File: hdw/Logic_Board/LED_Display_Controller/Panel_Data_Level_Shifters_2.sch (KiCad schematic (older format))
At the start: 62 parts, among them U2701 74HCT541, U2702 74HCT541

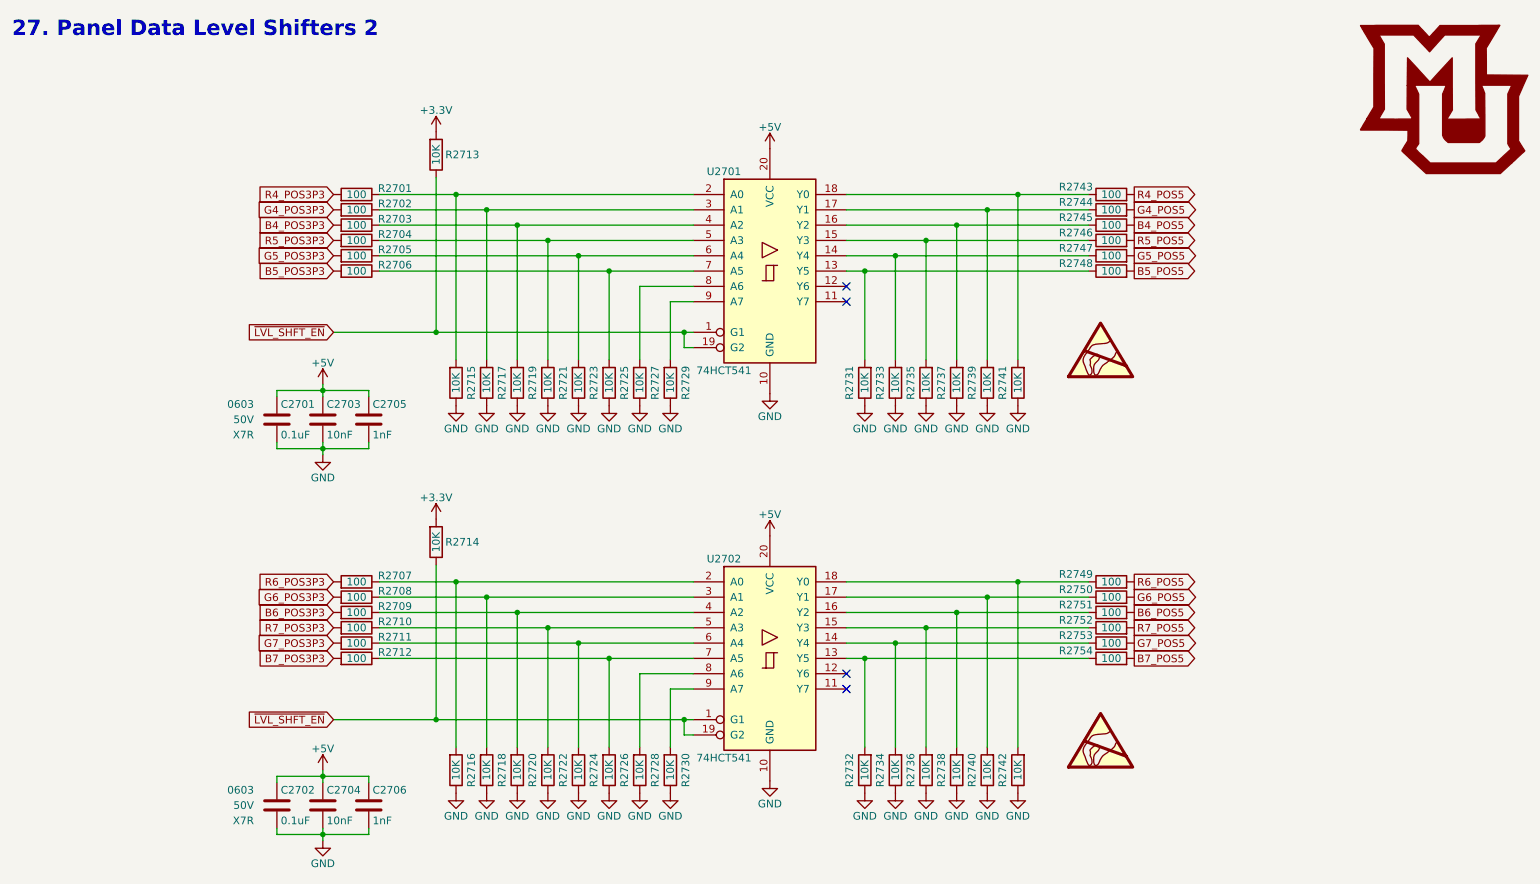
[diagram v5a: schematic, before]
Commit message: Resolved panel data connector orientation issues
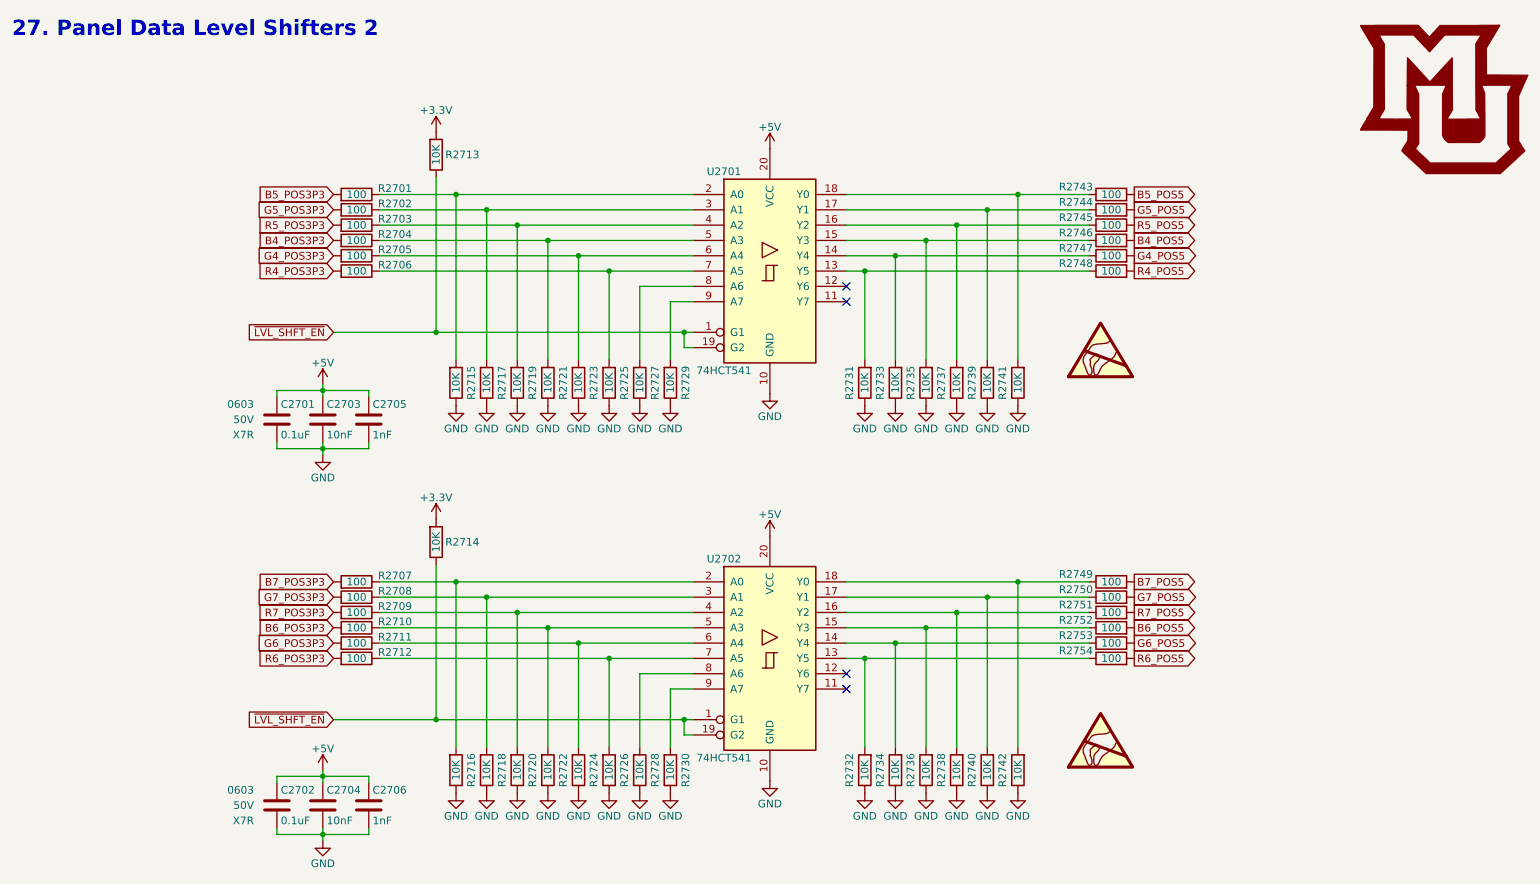
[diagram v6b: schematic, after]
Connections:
- net B4_POS3P3: now also R2704.1; no longer R2703.1
- net B4_POS5: now also R2746.1; no longer R2745.1
- net B5_POS3P3: now also R2701.1; no longer R2706.1
- net B5_POS5: now also R2743.1; no longer R2748.1
- net B6_POS3P3: now also R2710.1; no longer R2709.1
- net B6_POS5: now also R2752.1; no longer R2751.1
- net B7_POS3P3: now also R2707.1; no longer R2712.1
- net B7_POS5: now also R2749.1; no longer R2754.1
- net G4_POS3P3: now also R2705.1; no longer R2702.1
- net G4_POS5: now also R2747.1; no longer R2744.1
- net G5_POS3P3: now also R2702.1; no longer R2705.1
- net G5_POS5: now also R2744.1; no longer R2747.1
- net G6_POS3P3: now also R2711.1; no longer R2708.1
- net G6_POS5: now also R2753.1; no longer R2750.1
- net G7_POS3P3: now also R2708.1; no longer R2711.1
- net G7_POS5: now also R2750.1; no longer R2753.1
- net R4_POS3P3: now also R2706.1; no longer R2701.1
- net R4_POS5: now also R2748.1; no longer R2743.1
- net R5_POS3P3: now also R2703.1; no longer R2704.1
- net R5_POS5: now also R2745.1; no longer R2746.1
- net R6_POS3P3: now also R2712.1; no longer R2707.1
- net R6_POS5: now also R2754.1; no longer R2749.1
- net R7_POS3P3: now also R2709.1; no longer R2710.1
- net R7_POS5: now also R2751.1; no longer R2752.1
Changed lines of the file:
@@
 Wire Wire Line
 	4650 2320 4650 2800
+Text GLabel 7880 2220 2    50   Output ~ 0
+R4_POS5
+Text GLabel 7880 1920 2    50   Output ~ 0
+R5_POS5
+Text GLabel 7880 2020 2    50   Output ~ 0
+B4_POS5
 Text GLabel 7880 1720 2    50   Output ~ 0
-R4_POS5
-Text GLabel 7880 2020 2    50   Output ~ 0
-R5_POS5
-Text GLabel 7880 1920 2    50   Output ~ 0
-B4_POS5
-Text GLabel 7880 2220 2    50   Output ~ 0
 B5_POS5
+Text GLabel 7880 2120 2    50   Output ~ 0
+G4_POS5
 Text GLabel 7880 1820 2    50   Output ~ 0
-G4_POS5
-Text GLabel 7880 2120 2    50   Output ~ 0
 G5_POS5
 $Comp
@@
 Wire Wire Line
 	2950 2020 4050 2020
+Text GLabel 2650 2220 0    50   Input ~ 0
+R4_POS3P3
+Text GLabel 2650 1920 0    50   Input ~ 0
+R5_POS3P3
+Text GLabel 2650 2020 0    50   Input ~ 0
+B4_POS3P3
 Text GLabel 2650 1720 0    50   Input ~ 0
-R4_POS3P3
-Text GLabel 2650 2020 0    50   Input ~ 0
-R5_POS3P3
-Text GLabel 2650 1920 0    50   Input ~ 0
-B4_POS3P3
-Text GLabel 2650 2220 0    50   Input ~ 0
 B5_POS3P3
+Text GLabel 2650 2120 0    50   Input ~ 0
+G4_POS3P3
 Text GLabel 2650 1820 0    50   Input ~ 0
-G4_POS3P3
-Text GLabel 2650 2120 0    50   Input ~ 0
 G5_POS3P3
 Wire Wire Line
@@
 Wire Wire Line
 	4650 4850 4650 5330
+Text GLabel 7880 4750 2    50   Output ~ 0
+R6_POS5
+Text GLabel 7880 4450 2    50   Output ~ 0
+R7_POS5
+Text GLabel 7880 4550 2    50   Output ~ 0
+B6_POS5
 Text GLabel 7880 4250 2    50   Output ~ 0
-R6_POS5
-Text GLabel 7880 4550 2    50   Output ~ 0
-R7_POS5
-Text GLabel 7880 4450 2    50   Output ~ 0
-B6_POS5
-Text GLabel 7880 4750 2    50   Output ~ 0
 B7_POS5
+Text GLabel 7880 4650 2    50   Output ~ 0
+G6_POS5
 Text GLabel 7880 4350 2    50   Output ~ 0
-G6_POS5
-Text GLabel 7880 4650 2    50   Output ~ 0
 G7_POS5
 $Comp
@@
 Wire Wire Line
 	2950 4550 4050 4550
+Text GLabel 2650 4750 0    50   Input ~ 0
+R6_POS3P3
+Text GLabel 2650 4450 0    50   Input ~ 0
+R7_POS3P3
+Text GLabel 2650 4550 0    50   Input ~ 0
+B6_POS3P3
 Text GLabel 2650 4250 0    50   Input ~ 0
-R6_POS3P3
-Text GLabel 2650 4550 0    50   Input ~ 0
-R7_POS3P3
-Text GLabel 2650 4450 0    50   Input ~ 0
-B6_POS3P3
-Text GLabel 2650 4750 0    50   Input ~ 0
 B7_POS3P3
+Text GLabel 2650 4650 0    50   Input ~ 0
+G6_POS3P3
 Text GLabel 2650 4350 0    50   Input ~ 0
-G6_POS3P3
-Text GLabel 2650 4650 0    50   Input ~ 0
 G7_POS3P3
 Wire Wire Line
